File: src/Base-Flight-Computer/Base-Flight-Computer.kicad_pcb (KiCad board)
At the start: 4 copper layers, 66.8 x 25.4 mm, 61 parts, among them J1 Jumper_NO, P1 CONN_1984659_PXC, P2 USB, P3 0530470610, P4 1546551-2, Q1 QS5U17TR, Q2 2N7002W-7-F, Q3 2N7002W-7-F, Q4 QS5U17TR, Q5 2N7002W-7-F, Q6 2N7002W-7-F, U1 STM32G4A1KEU6, U2 BMP390, U3 LMS8117AMP-3.3_NOPB, U4 SST25VF040B-50-4I-S2AE-T, Y1 ECS-240-18-33-JGN-TR

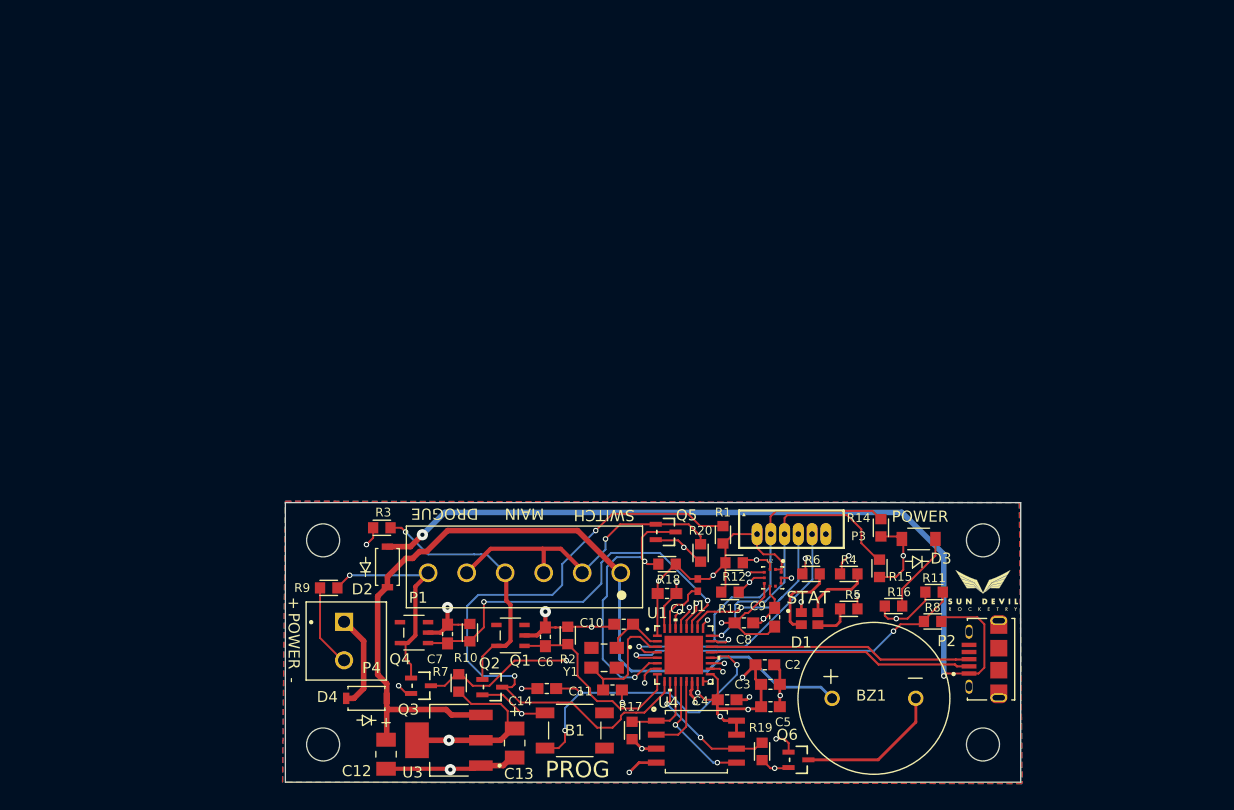
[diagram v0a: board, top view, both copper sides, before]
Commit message: added four terminal screw terminal to lib files
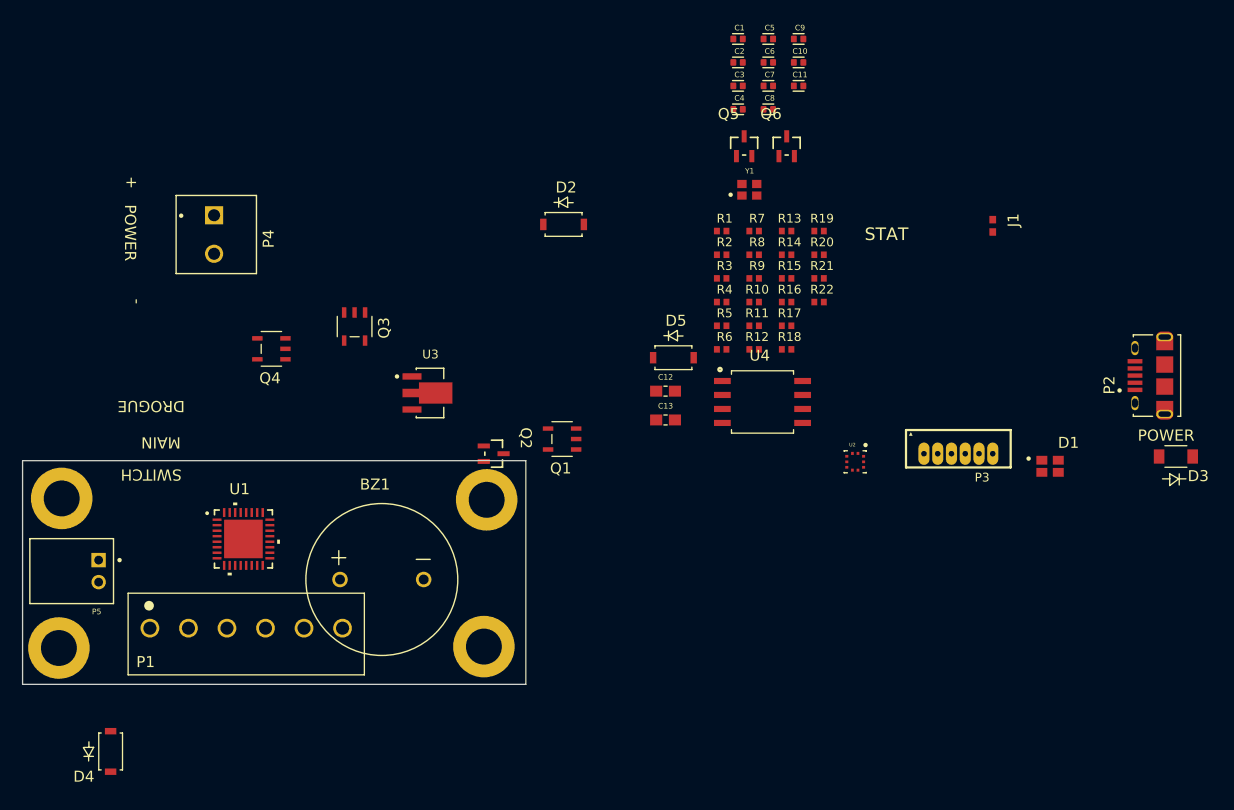
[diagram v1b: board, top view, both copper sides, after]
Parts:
- removed B1: PTS647SM38SMTR2LFS, Flight-Computer-Lite:PTS647SM38SMTR2LFS
- removed C14: 0.1uF, Flight-Computer-Lite:CAP_0603
- removed LOGO1: Logo, Flight-Computer-Lite:logo_small
- added D5: SM5819PL-TP, Base-Flight-Computer:SM5819PL-TP, F.Cu at (186.1, 71.9)
- added P5: 1984659, Base-Flight-Computer:JST_S2B-PH-K-S(LF)(SN), F.Cu at (133.9, 91.3)
- added R21: 39k, Base-Flight-Computer:RES_0402, F.Cu at (199.4, 64.7)
- added R22: 10k, Base-Flight-Computer:RES_0402, F.Cu at (199.4, 66.9)
- BZ1: footprint Flight-Computer-Lite:AT-1438-TWT-R -> Base-Flight-Computer:AT-1438-TWT-R
- C1, C2, C3, C5, C6, C7, C8, C9: footprint Flight-Computer-Lite:CAP_0603 -> Base-Flight-Computer:CAP_0402
- C10, C11: value 8pF -> 4pF; footprint Flight-Computer-Lite:CAP_0603 -> Base-Flight-Computer:CAP_0402
- C12, C13: value 10uF -> 1uF; footprint Flight-Computer-Lite:T491A106K010AT -> Base-Flight-Computer:CAP_0603
- C4: value 0.01uF -> 10nF; footprint Flight-Computer-Lite:CAP_0603 -> Base-Flight-Computer:CAP_0402
- D1: footprint Flight-Computer-Lite:CLMVC-FKA-CL1D1L71BB7C3C3 -> Base-Flight-Computer:CLMVC-FKA-CL1D1L71BB7C3C3
- D2, D4: footprint Flight-Computer-Lite:SM5819PL-TP -> Base-Flight-Computer:SM5819PL-TP
- H1, H2, H3, H4: value Mounting-Hole -> Mounting-Hole-4-40; footprint Flight-Computer-Lite:MountingHole_3mm -> Base-Flight-Computer:MountingHole_4-40
- J1: footprint Flight-Computer-Lite:Jumper-NO -> Base-Flight-Computer:Jumper-NO
- P1: value CONN_1984659_PXC -> 1984659; footprint Flight-Computer-Lite:1984659 -> Base-Flight-Computer:1984659
- P2: footprint Flight-Computer-Lite:10118194-0001LF -> Base-Flight-Computer:10118194-0001LF
- P3: footprint Flight-Computer-Lite:53047-0610 -> Base-Flight-Computer:53047-0610
- P4: footprint Flight-Computer-Lite:1546551-2 -> Base-Flight-Computer:1546551-2
- Q1, Q4: footprint Flight-Computer-Lite:QS5U17TR -> Base-Flight-Computer:QS5U17TR
- Q2, Q5, Q6: footprint Flight-Computer-Lite:2N7002W-7-F -> Base-Flight-Computer:2N7002W-7-F
- Q3: footprint Flight-Computer-Lite:2N7002W-7-F -> Base-Flight-Computer:QS5U17TR
- R1, R10, R12, R13, R14, R15, R16, R17, R18, R19, R2, R5, R7: footprint Flight-Computer-Lite:RES_0603 -> Base-Flight-Computer:RES_0402
- R11: value 20k -> 200k; footprint Flight-Computer-Lite:RES_0603 -> Base-Flight-Computer:RES_0402
- R20, R3, R8, R9: value 10k -> 100k; footprint Flight-Computer-Lite:RES_0603 -> Base-Flight-Computer:RES_0402
- R4: value 68 -> 82; footprint Flight-Computer-Lite:RES_0603 -> Base-Flight-Computer:RES_0402
- R6: value 280 -> 240; footprint Flight-Computer-Lite:RES_0603 -> Base-Flight-Computer:RES_0402
- U1: footprint Flight-Computer-Lite:STM32G4A1KEU6 -> Base-Flight-Computer:STM32G4A1KEU6
- U2: footprint Flight-Computer-Lite:BMP390 -> Base-Flight-Computer:BMP390
- U3: footprint Flight-Computer-Lite:LMS8117AMP-3.3NOPB -> Base-Flight-Computer:AP7370-33Y-13
- U4: footprint Flight-Computer-Lite:SST25VF040B-50-4I-S2AE-T -> Base-Flight-Computer:SST25VF040B-50-4I-S2AE-T
- Y1: footprint Flight-Computer-Lite:ECS-240-18-33-JGN-TR -> Base-Flight-Computer:ECS-240-12-37B-CKY-TR
- moved H2 86.6 mm to (130.6, 84.7)
- moved C5 60.7 mm to (194.8, 43.0)
- moved C7 57.7 mm to (194.8, 47.2), turned to 0 degrees
- moved C11 57.4 mm to (197.5, 47.2)
- moved C6 56.0 mm to (194.8, 45.1), turned to 0 degrees
- moved Q6 55.8 mm to (196.4, 52.7), turned to 0 degrees
- moved C2 54.8 mm to (192.0, 45.1)
- moved C3 54.4 mm to (192.0, 47.2)
- moved C4 53.6 mm to (192.0, 49.4)
- moved C10 53.5 mm to (197.5, 45.1), turned to 0 degrees
- moved C9 52.6 mm to (197.5, 43.0), turned to 0 degrees
- moved C1 50.8 mm to (192.0, 43.0)
- moved R7 49.0 mm to (193.5, 60.4), turned to 0 degrees
- moved R9 47.8 mm to (193.5, 64.7)
- moved R19 47.6 mm to (199.4, 60.4), turned to 0 degrees
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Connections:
- R8 pad 1: USB_DETECT -> 5V
- R8 pad 2: 5V -> USB_DETECT
- U1 pad 20: PROG -> USB_DETECT
- U1 pad 5: USB_DETECT -> VBAT_SENSE
- U3 pad 1: Earth -> 3.3V
- U3 pad 2: 3.3V -> Earth
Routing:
- net Earth: track 86.2 -> 0.00 mm, vias 21 -> 0
- net VIN: track 77.6 -> 0.00 mm
- net 5V: track 76.4 -> 0.00 mm, vias 2 -> 0
- net 3.3V: track 73.0 -> 0.00 mm, vias 12 -> 0
- net ~{MAIN_CONT}: track 58.9 -> 0.00 mm, vias 2 -> 0
- net DROGUE: track 36.1 -> 0.00 mm, vias 2 -> 0
- net USB_DETECT: track 32.3 -> 0.00 mm, vias 2 -> 0
- net ~{DROGUE_CONT}: track 30.4 -> 0.00 mm, vias 2 -> 0
- net PROG: track 29.5 -> 0.00 mm, vias 3 -> 0
- net VIN_SW: track 28.8 -> 0.00 mm, vias 1 -> 0
- net SWDIO: track 28.4 -> 0.00 mm, vias 1 -> 0
- net STATUS_B: track 27.1 -> 0.00 mm, vias 2 -> 0
- net SWCLK: track 26.9 -> 0.00 mm, vias 1 -> 0
- net ~{SWITCH}: track 25.3 -> 0.00 mm, vias 2 -> 0
- net STATUS_G: track 24.7 -> 0.00 mm, vias 2 -> 0
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- removed copper zone on In2.Cu, net 3.3V
- removed copper zone on B.Cu, net Earth
- removed copper zone on F.Cu, net Earth
- removed copper zone on In1.Cu, net Earth
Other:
- board size 66.8 x 25.4 mm -> 45.7 x 20.3 mm
- board text removed: "A0007 Flight Computer Lite Rev 2.0"
- board text removed: "PROG"

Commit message: replaced green power indication LED with smaller 0603 alternate
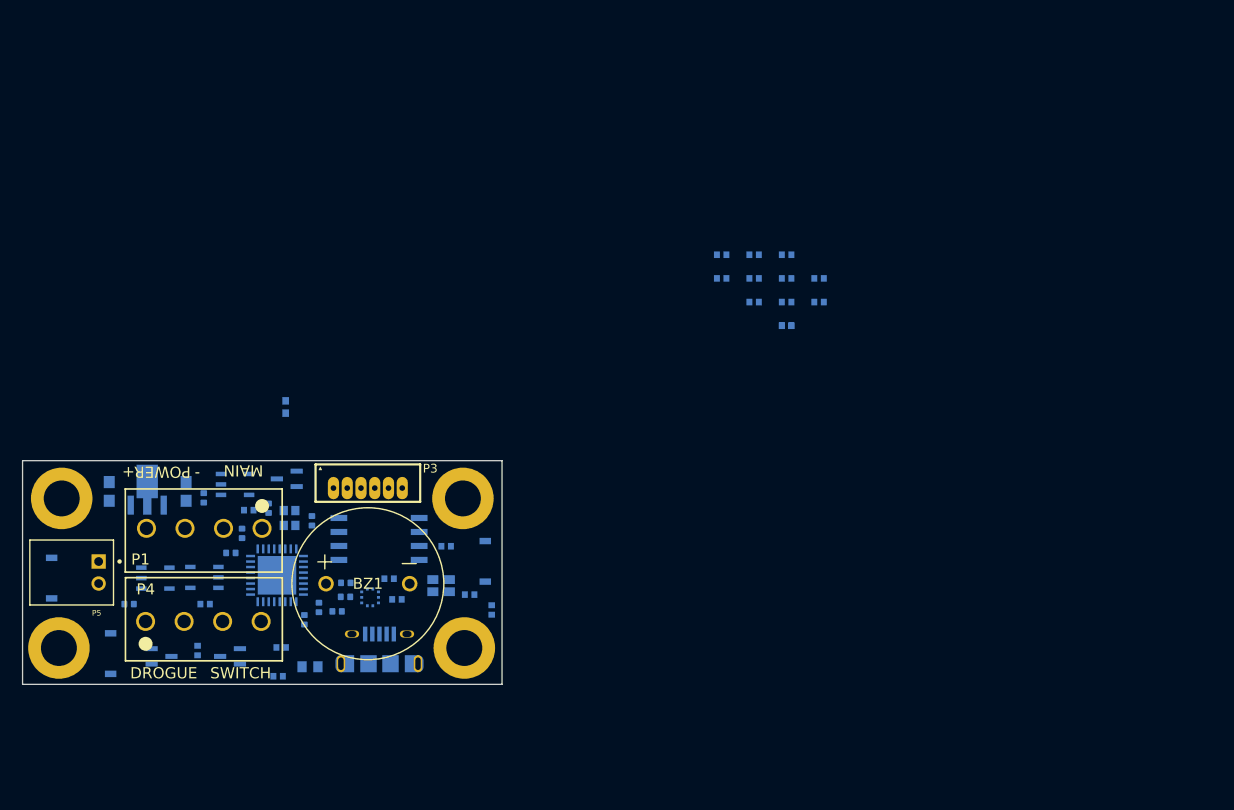
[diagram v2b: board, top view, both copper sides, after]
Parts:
- C1, C10, C11, C12, C13, C2, C3, C4, C5, C6, C7, C8, C9, D1, D2, D4, D5, J1, P2, Q1, Q2, Q3, Q4, Q5, Q6, R1, R10, R11, R12, R13, R14, R15, R16, R17, R18, R19, R2, R20, R21, R22, R3, R4, R5, R6, R7, R8, R9, U1, U2, U3, U4, Y1: moved to B.Cu
- D3: value SML-LX1206GC-TR -> LTST-C191KGKT; footprint Flight-Computer:SML-LX1206GC-TR -> Base-Flight-Computer:LTST-C191KGKT; moved to B.Cu
- P1: footprint Base-Flight-Computer:1984659 -> Base-Flight-Computer:1546551-4
- P4: value 1546551-2 -> 1984659; footprint Base-Flight-Computer:1546551-2 -> Base-Flight-Computer:1546551-4
- moved D3 80.9 mm to (153.1, 100.0)
- moved P2 76.0 mm to (159.4, 99.7), turned to 180 degrees
- moved C7 74.8 mm to (136.7, 94.3), turned to 180 degrees
- moved Q6 73.3 mm to (139.6, 99.1), turned to 90 degrees
- moved J1 66.3 mm to (150.9, 76.4)
- moved Q5 65.8 mm to (145.8, 99.1), turned to -90 degrees
- moved C9 65.3 mm to (156.3, 93.6), turned to 180 degrees
- moved C5 65.1 mm to (155.6, 95.0)
- moved C6 64.8 mm to (143.5, 84.7), turned to 90 degrees
- moved C1 64.2 mm to (153.9, 94.6), turned to -90 degrees
- moved C10 62.9 mm to (149.4, 85.6), turned to 90 degrees
- moved C3 62.6 mm to (145.9, 89.7), turned to 180 degrees
- moved C2 62.1 mm to (146.9, 87.9), turned to 90 degrees
- moved C4 60.8 mm to (152.6, 95.7), turned to -90 degrees
- moved R20 60.5 mm to (150.5, 98.2), turned to 180 degrees
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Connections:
- D4 pad 2: Net-(P4-5) -> Net-(P1A-5)
- P1 pad 1: VIN -> Net-(P1A-5)
- P1 pad 2: VIN_SW -> Earth
- P4 pad 1: Net-(P4-5) -> VIN_SW
- P4 pad 2: Earth -> Net-(P4A-6)
- Q3 pad 1: Net-(Q3-G) -> Net-(P4A-6)
- Q4 pad 5: Net-(Q3-G) -> Net-(P4A-6)
- R9 pad 2: Net-(Q3-G) -> Net-(P4A-6)
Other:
- board size 45.7 x 20.3 mm -> 43.6 x 20.3 mm
- board text added: "RST"

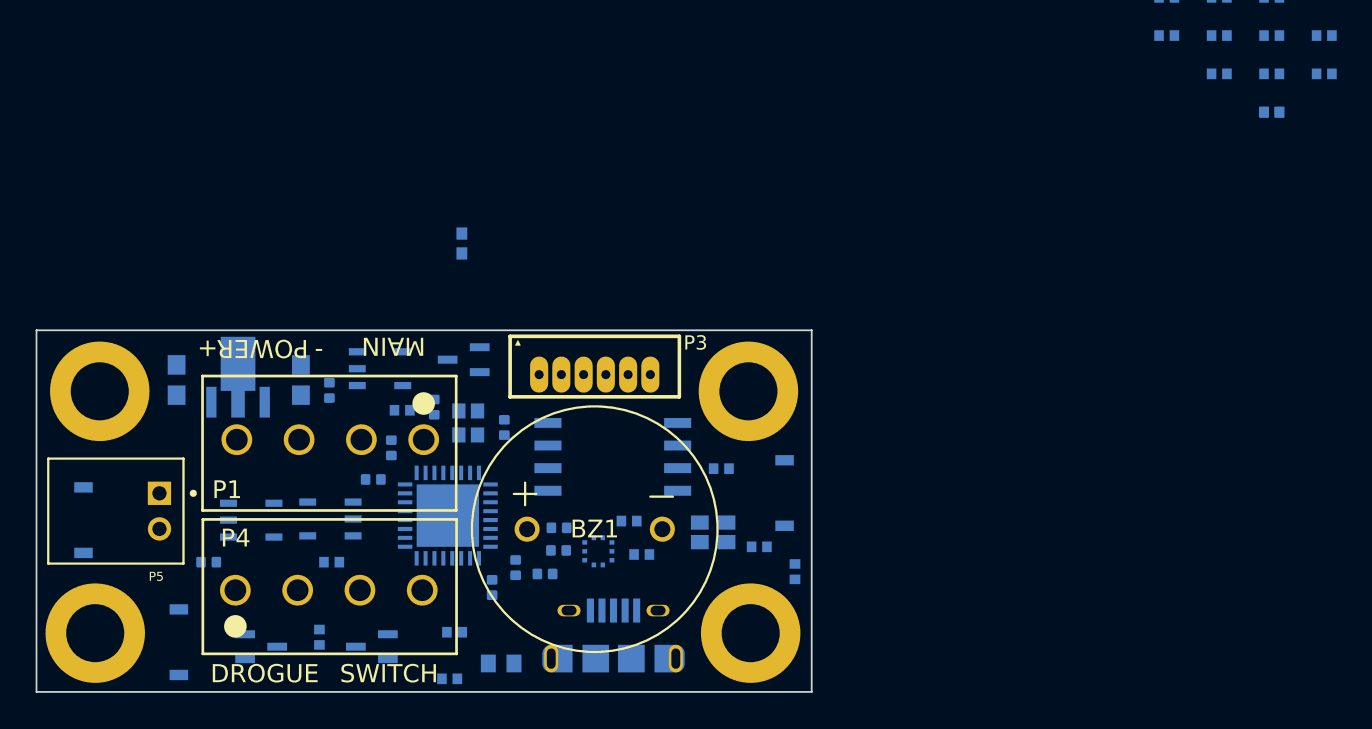
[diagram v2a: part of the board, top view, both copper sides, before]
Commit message: replaced schottky diode with smaller form factor diode
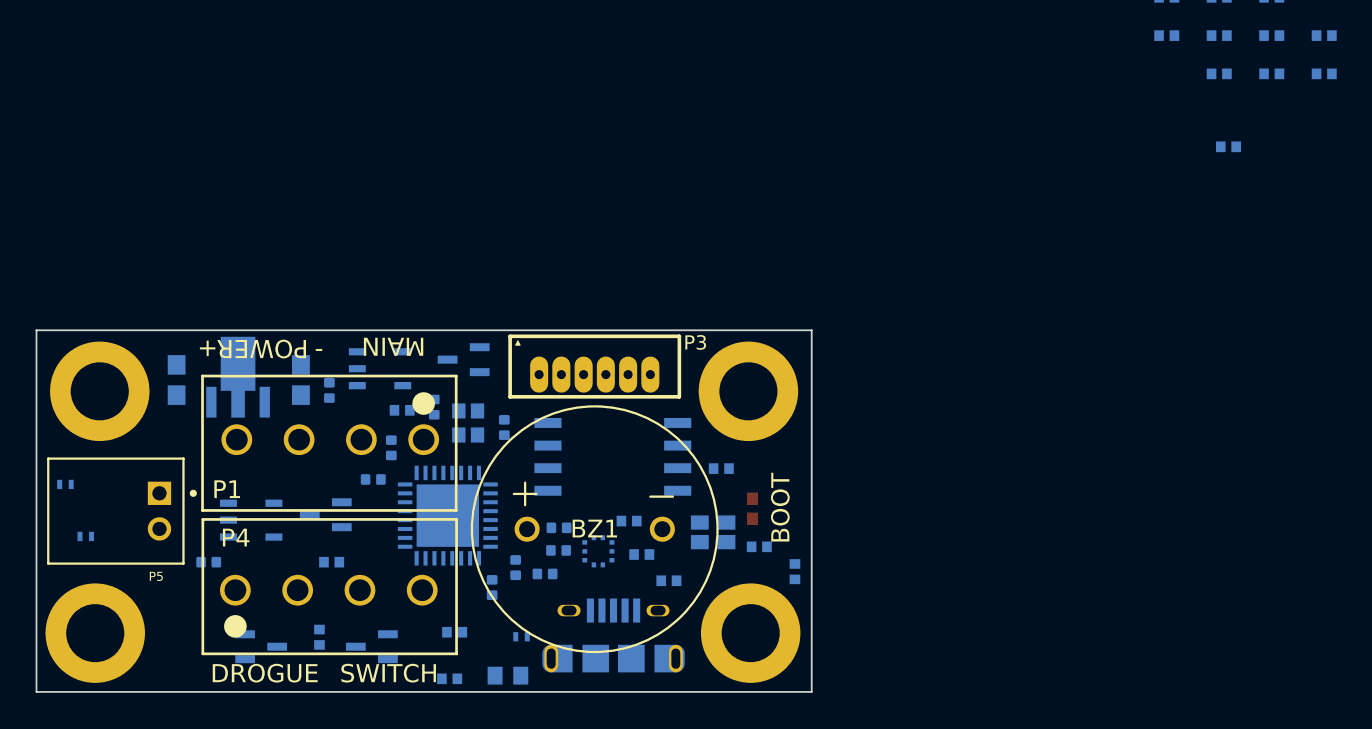
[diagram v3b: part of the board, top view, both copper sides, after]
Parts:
- D2, D4, D5: value SM5819PL-TP -> PMEG3010AESBYL; footprint Base-Flight-Computer:SM5819PL-TP -> Base-Flight-Computer:PMEG3010AESBYL
- J1: moved to F.Cu
- Q3: footprint Base-Flight-Computer:QS5U17TR -> Base-Flight-Computer:2N7002W-7-F
- moved R6 42.9 mm to (162.5, 95.4)
- moved J1 22.1 mm to (167.2, 91.3)
- moved D2 16.8 mm to (154.3, 98.5), turned to 180 degrees
- moved D4 7.92 mm to (129.8, 92.9), turned to 180 degrees
- moved R17 3.11 mm to (194.0, 71.0)
- moved D5 2.25 mm to (128.6, 89.9), turned to 180 degrees
- moved D3 0.78 mm to (153.5, 100.7)
- moved Q3 0.35 mm to (143.3, 91.6), turned to -90 degrees
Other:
- board text added: "BOOT"
